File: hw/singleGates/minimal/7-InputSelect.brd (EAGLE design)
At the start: 32 parts, among them Q1 BC817, Q10 BC817, Q11 BC817, Q12 BC817, Q13 BC817, Q14 BC817, Q17 BC817, Q2 BC817, Q3 BC817, Q4 BC817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

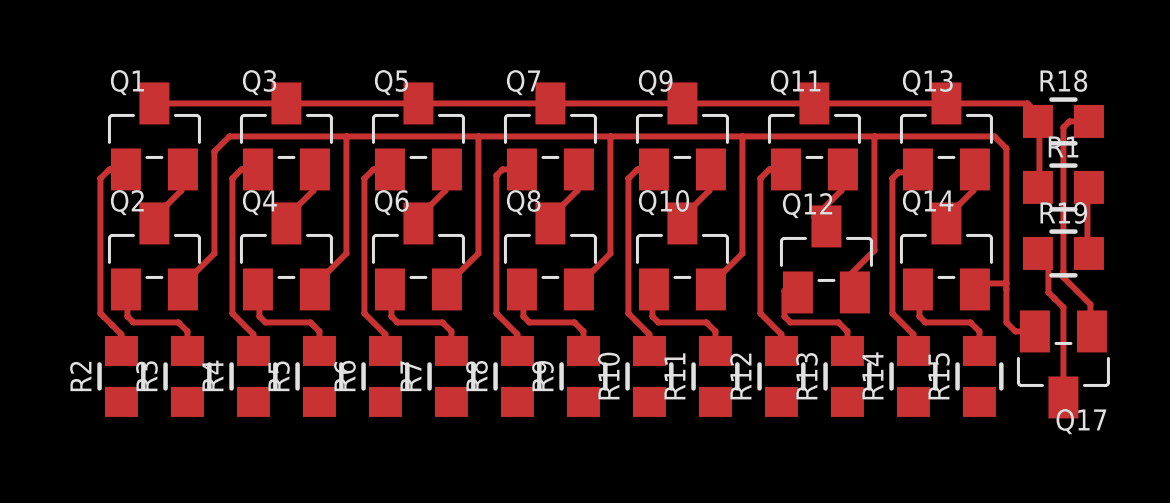
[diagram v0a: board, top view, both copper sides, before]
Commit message: Add led output and prepare first alu slice
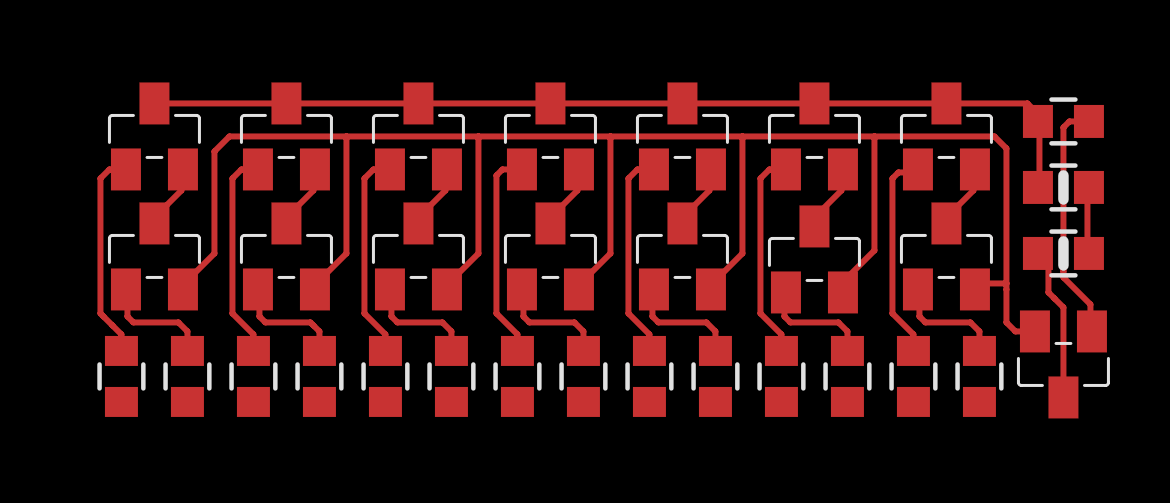
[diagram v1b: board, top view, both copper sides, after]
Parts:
- R1, R19: device p.peter-gator:R0603 -> p.peter-rcl:R0603-MARK
- moved Q12 0.40 mm to (24.3, 5.60)
